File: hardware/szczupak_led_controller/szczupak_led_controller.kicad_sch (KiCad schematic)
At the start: 0 parts

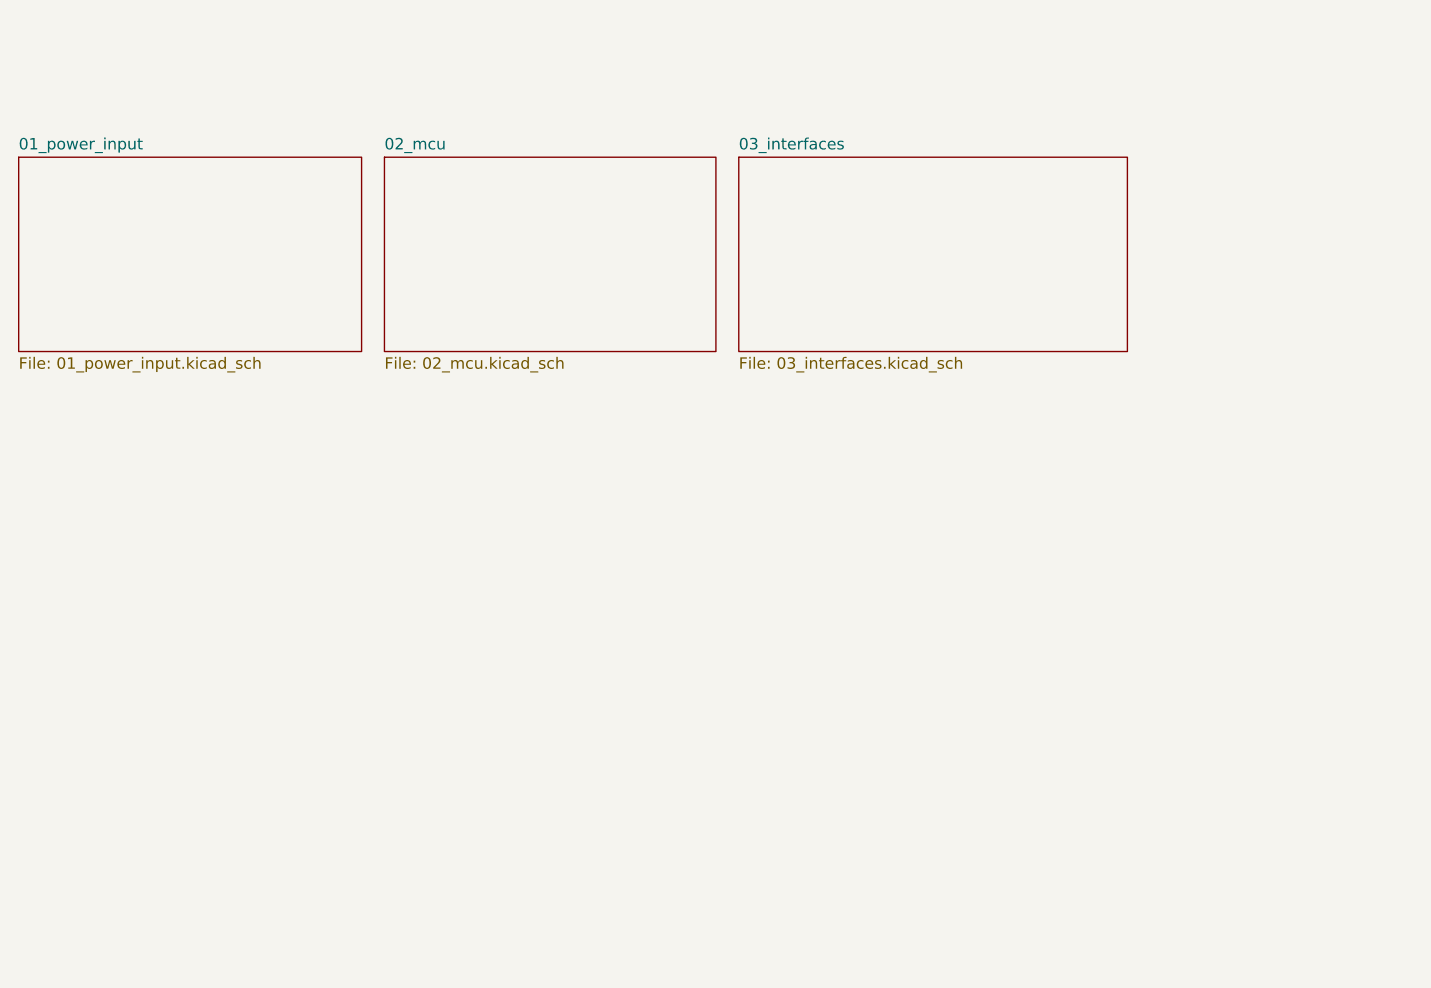
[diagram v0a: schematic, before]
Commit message: #4 #6 Added power output and interfaces schematics
Designed initial placement for most important components on pcb
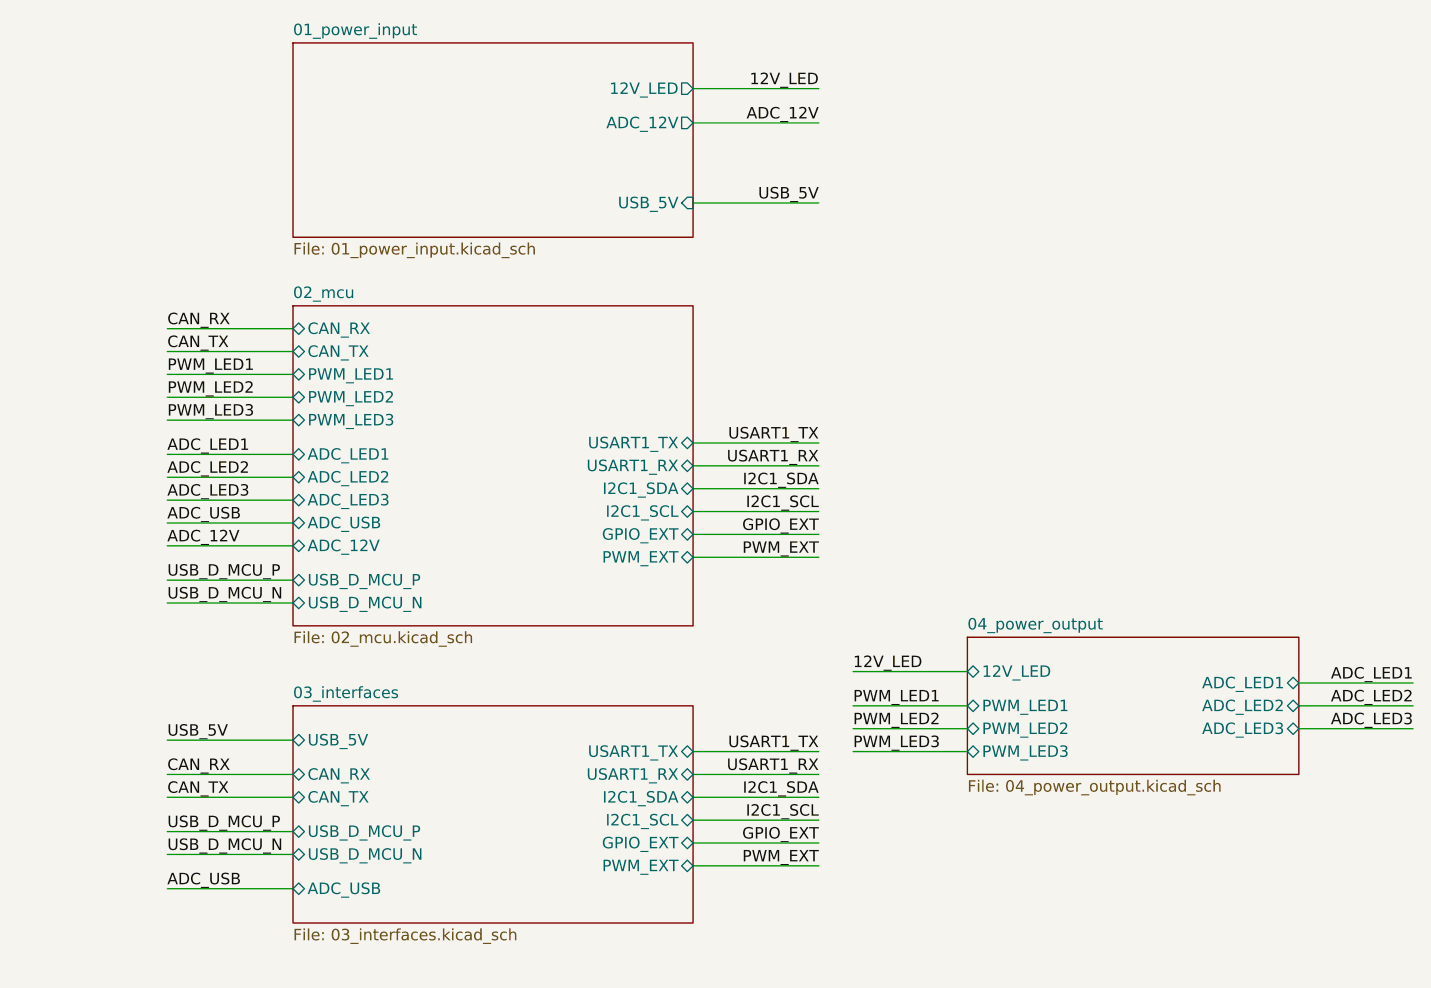
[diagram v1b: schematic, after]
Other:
- added sheet 04_power_output (04_power_output.kicad_sch)
- sheet 01_power_input ports: added 12V_LED, ADC_12V, USB_5V; removed none
- sheet 02_mcu ports: added ADC_12V, ADC_LED1, ADC_LED2, ADC_LED3, ADC_USB, CAN_RX, CAN_TX, GPIO_EXT, I2C1_SCL, I2C1_SDA, PWM_EXT, PWM_LED1, PWM_LED2, PWM_LED3, USART1_RX, USART1_TX, USB_D_MCU_N, USB_D_MCU_P; removed none
- sheet 03_interfaces ports: added ADC_USB, CAN_RX, CAN_TX, GPIO_EXT, I2C1_SCL, I2C1_SDA, PWM_EXT, USART1_RX, USART1_TX, USB_5V, USB_D_MCU_N, USB_D_MCU_P; removed none
- company: (none) -> AGH Marines

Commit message: #8 Finished initial component placement on pcb
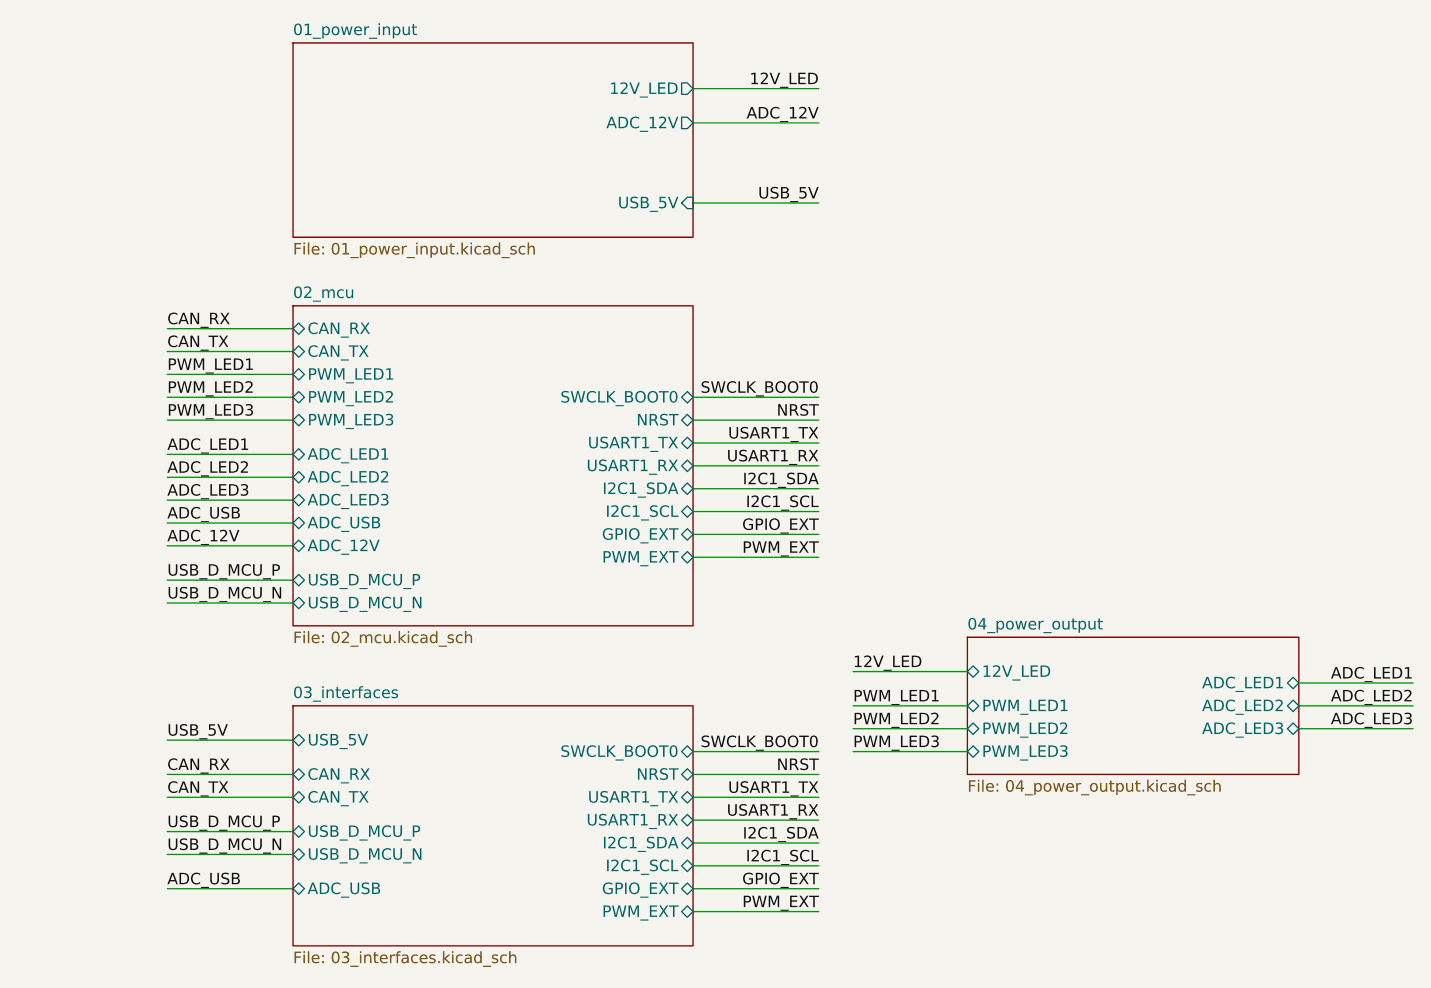
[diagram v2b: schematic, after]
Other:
- sheet 02_mcu ports: added NRST, SWCLK_BOOT0; removed none
- sheet 03_interfaces ports: added NRST, SWCLK_BOOT0; removed none
